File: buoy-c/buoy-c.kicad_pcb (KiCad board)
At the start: 4 copper layers, 51.2 x 97.5 mm, 78 parts, among them J1 Conn_01x06_Male, J10 Conn_01x06_Male, J11 TERM-BLK-2P, J12 Conn_01x04_Male, J2 BAT-HLD-001-THM, J3 Conn_01x02_Male, J4 U.FL-R-SMT-1_10_, J5 BH-18650-PC, J6 Conn_01x06_Male, J7 Conn_01x02_Male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

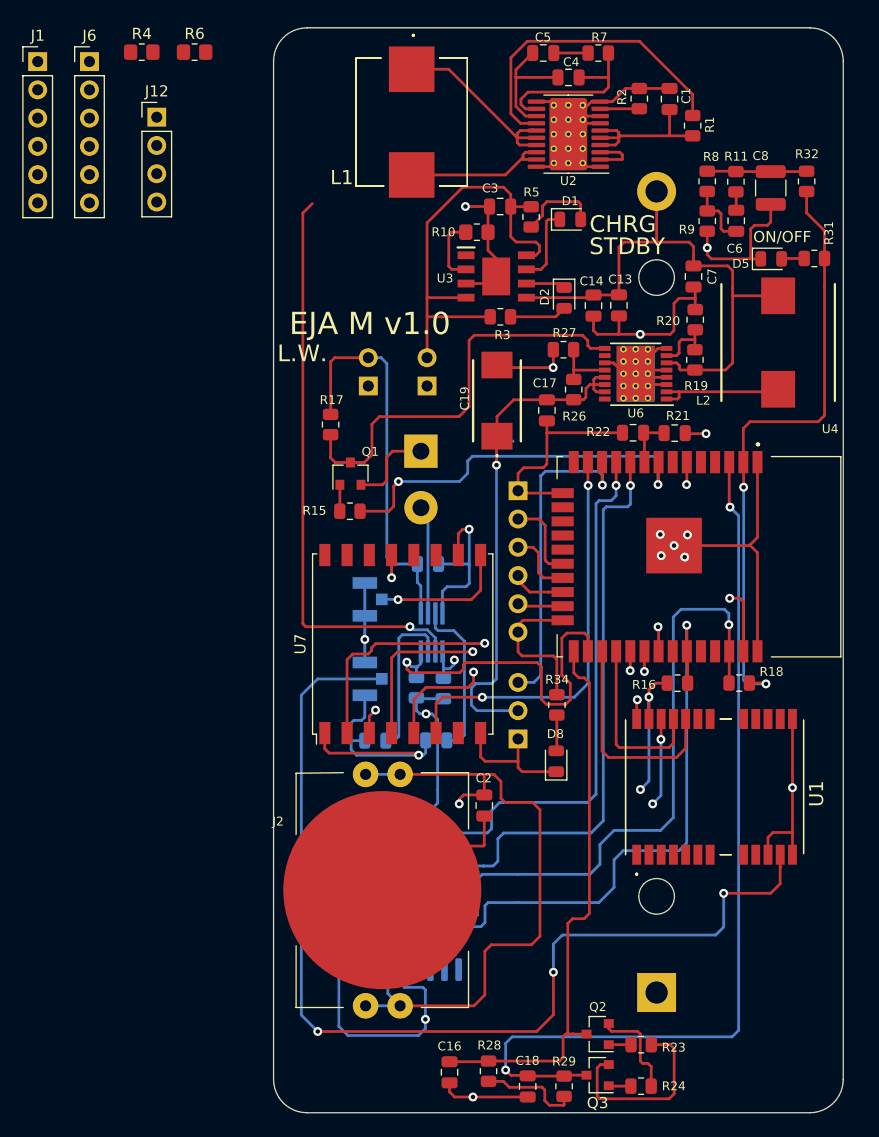
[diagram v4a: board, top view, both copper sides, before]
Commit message: Changed routing of the sepic converter
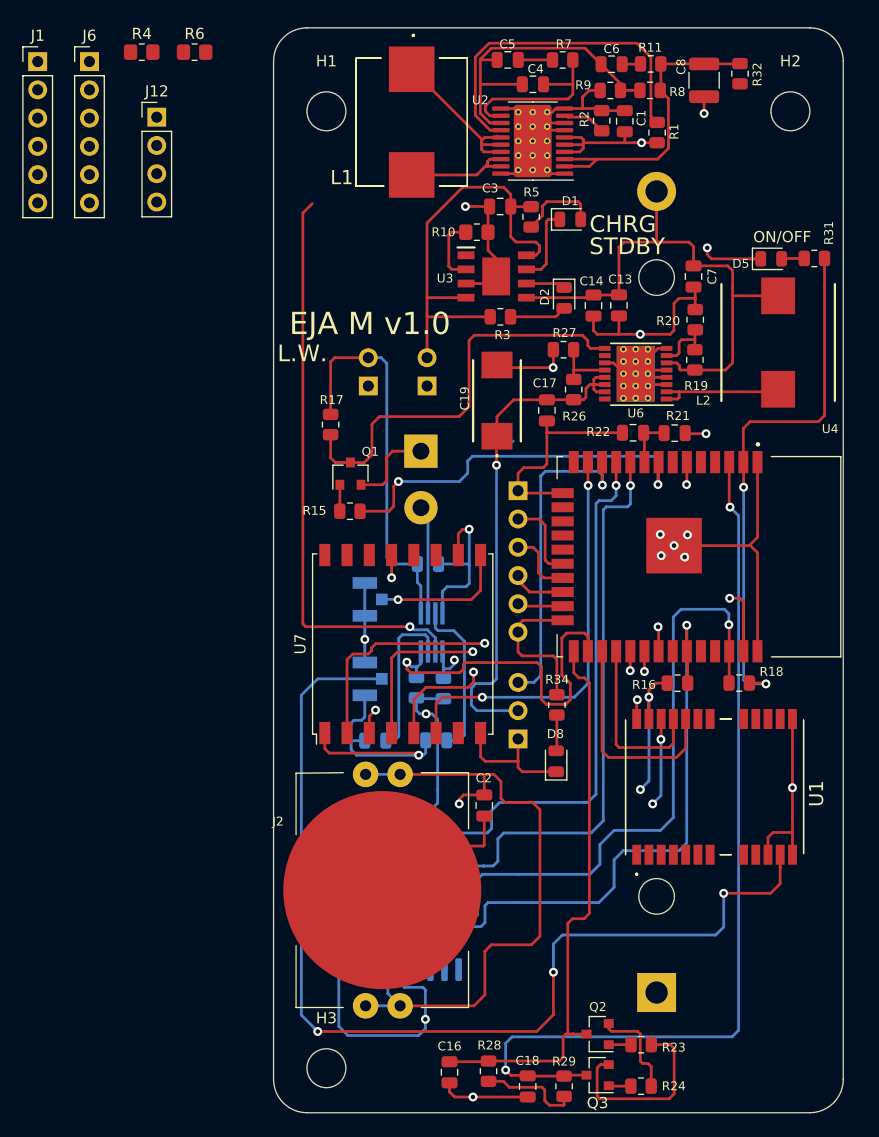
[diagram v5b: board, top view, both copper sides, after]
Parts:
- added H1: MountingHole, MountingHole:MountingHole_3.5mm, F.Cu at (105.3, 107.5)
- added H2: MountingHole, MountingHole:MountingHole_3.5mm, F.Cu at (147.0, 107.5)
- added H3: MountingHole, MountingHole:MountingHole_3.5mm, F.Cu at (105.3, 193.5)
- moved C6 18.0 mm to (130.9, 103.3), turned to 180 degrees
- moved R9 14.6 mm to (130.8, 105.6), turned to 180 degrees
- moved R11 13.1 mm to (134.4, 103.2), turned to 180 degrees
- moved C8 11.4 mm to (139.2, 104.7)
- moved R32 11.4 mm to (142.5, 104.1)
- moved R8 9.65 mm to (134.4, 105.6), turned to 180 degrees
- moved C1 4.49 mm to (132.1, 108.4)
- moved R2 3.92 mm to (130.0, 108.3)
- moved C5 3.26 mm to (121.6, 102.9)
- moved C4 3.26 mm to (123.9, 105.1)
- moved R1 3.26 mm to (135.0, 109.4)
- moved R7 3.26 mm to (126.5, 102.9)
- moved U2 3.26 mm to (123.8, 110.2)
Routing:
- net +3V3: track 13.5 -> 28.0 mm
- net Net-(C4-Pad1): track 17.3 -> 29.1 mm
- net VDD: track 148.3 -> 141.6 mm
- net GND: track 278.5 -> 273.8 mm, vias 16 -> 17
- net EN_3V3: track 80.3 -> 82.8 mm
- net Net-(L1-Pad1): track 18.6 -> 16.2 mm
- net Net-(L1-Pad2): track 13.6 -> 12.1 mm
- net +BATT: track 132.7 -> 131.4 mm, vias 1 -> 2

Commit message: Changed toutes of the PCB, including routes width
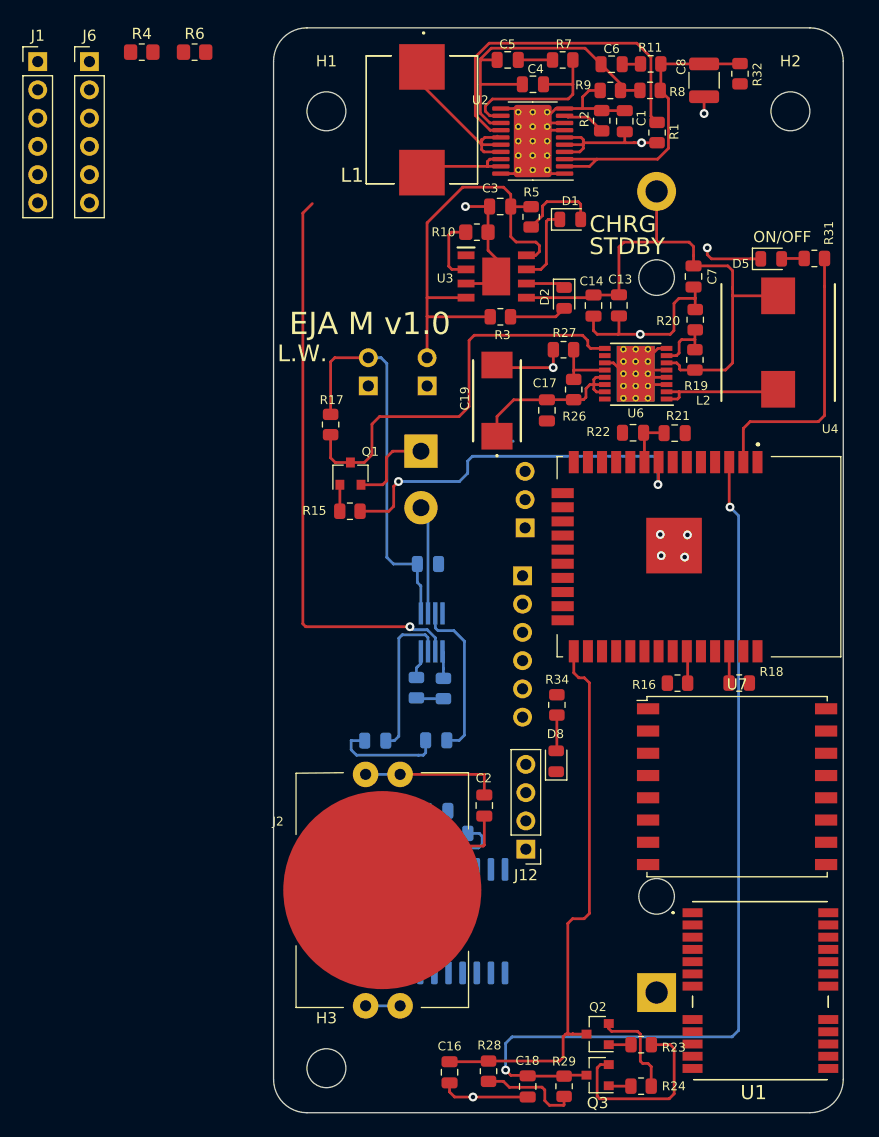
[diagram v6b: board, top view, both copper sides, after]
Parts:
- moved J12 73.7 mm to (123.2, 173.8), turned to 180 degrees
- moved U7 32.7 mm to (142.2, 168.2), turned to 0 degrees
- moved J4 21.8 mm to (108.6, 180.3)
- moved J9 21.8 mm to (108.6, 173.2)
- moved J8 19.0 mm to (123.2, 144.9)
- moved U1 18.8 mm to (144.3, 186.5), turned to 180 degrees
- moved J10 7.66 mm to (122.9, 149.3)
- moved C15 4.18 mm to (115.3, 170.4)
- moved U8 4.18 mm to (116.9, 180.3)
- moved R25 4.18 mm to (117.1, 172.4)
- moved L1 0.94 mm to (113.9, 108.3)
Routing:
- net GND: track 273.8 -> 123.6 mm, vias 17 -> 10
- net VDD: track 141.6 -> 34.9 mm, vias 6 -> 0
- net Net-(J4-Pad3): track 94.0 -> 0.00 mm, vias 3 -> 0
- net LORA_MOSI: track 83.9 -> 0.00 mm, vias 2 -> 0
- net BAT-CR2032: track 83.7 -> 16.2 mm, vias 3 -> 0
- net SCL: track 68.8 -> 2.86 mm, vias 1 -> 0
- net RST_RTC: track 59.4 -> 0.00 mm, vias 1 -> 0
- net SDA: track 62.0 -> 2.89 mm, vias 1 -> 0
- net INT_RTC: track 56.4 -> 8.35 mm, vias 1 -> 0
- net LORA_MISO: track 39.1 -> 0.00 mm, vias 2 -> 0
- net BUTTON_INT: track 41.3 -> 2.46 mm, vias 2 -> 0
- net LORA_RST: track 37.0 -> 0.00 mm, vias 2 -> 0
- net +BATT: track 131.4 -> 97.7 mm, vias 2 -> 1
- net LORA_SCK: track 33.1 -> 0.00 mm, vias 2 -> 0
- net BUTTON_KILL: track 32.9 -> 2.51 mm, vias 1 -> 0
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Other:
- board text removed: "SCL"
- board text removed: "SDA"
- board text removed: "VDD"
